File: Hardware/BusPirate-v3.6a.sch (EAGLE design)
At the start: 46 parts, among them IC1 4066, J1 USB-MINIB-5PIN, U1 MIC5205 3V3, U2 MIC5205 3V3, U3 PIC24FJ64GA002, U4 MIC5205 5V0, U5 FT232RL-BASICSSOP

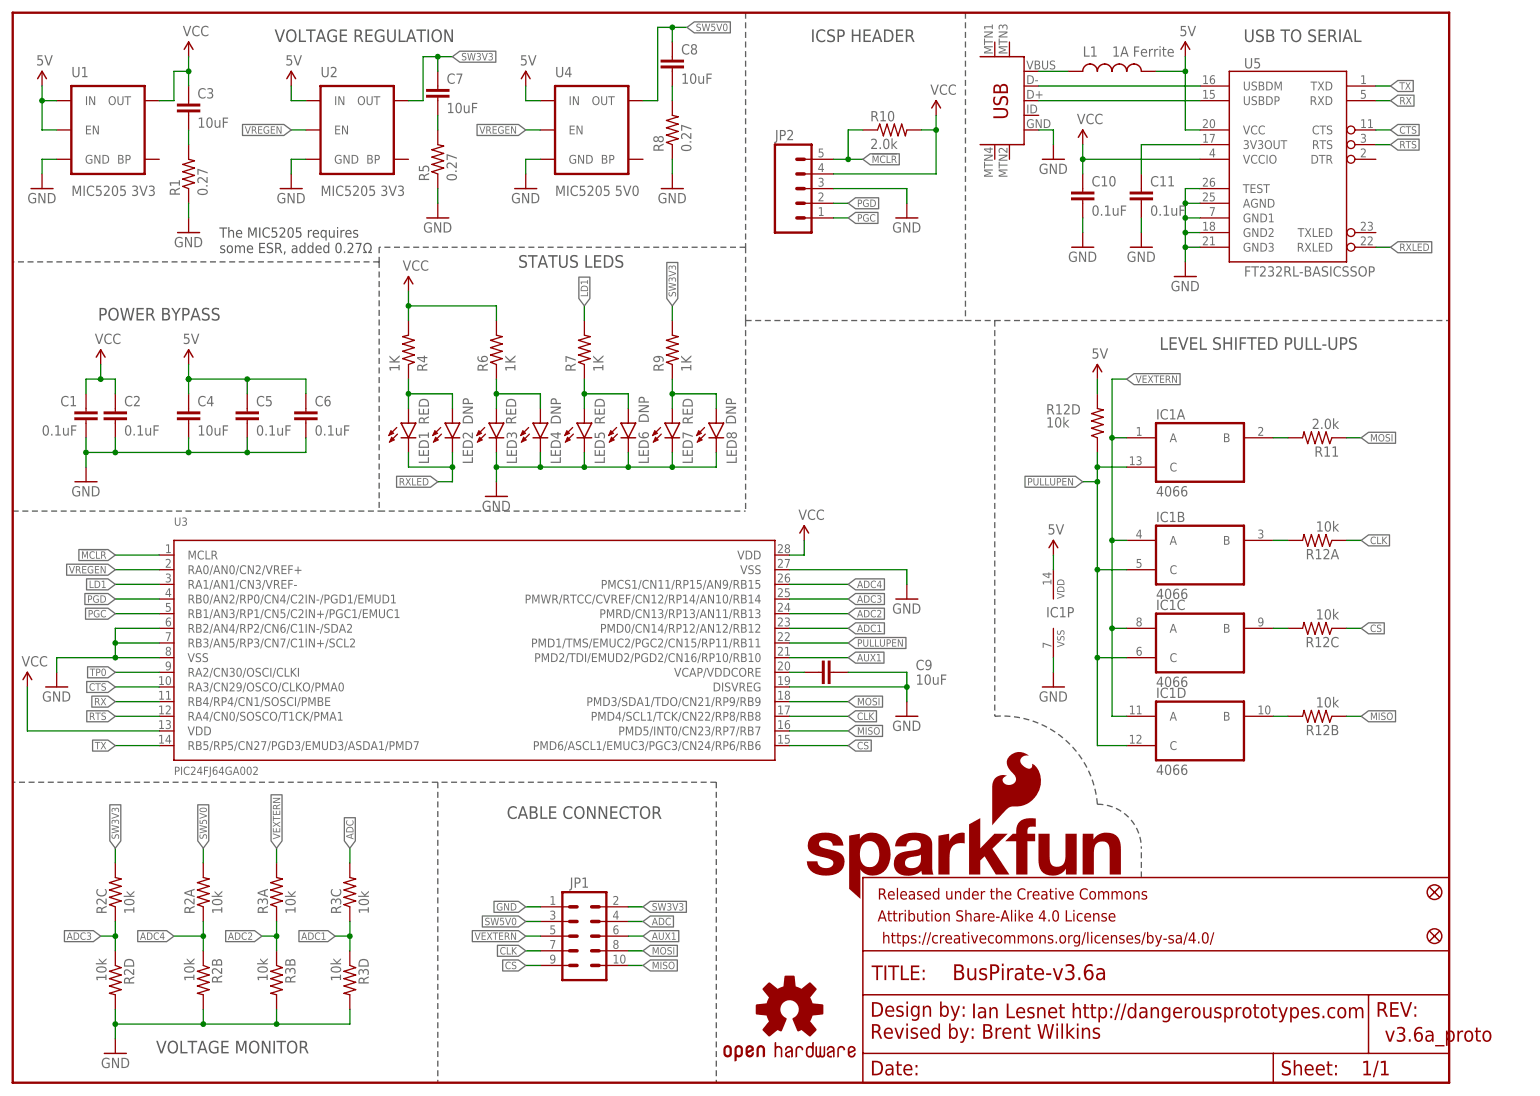
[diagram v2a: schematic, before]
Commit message: Changed license from CC4 to CC0
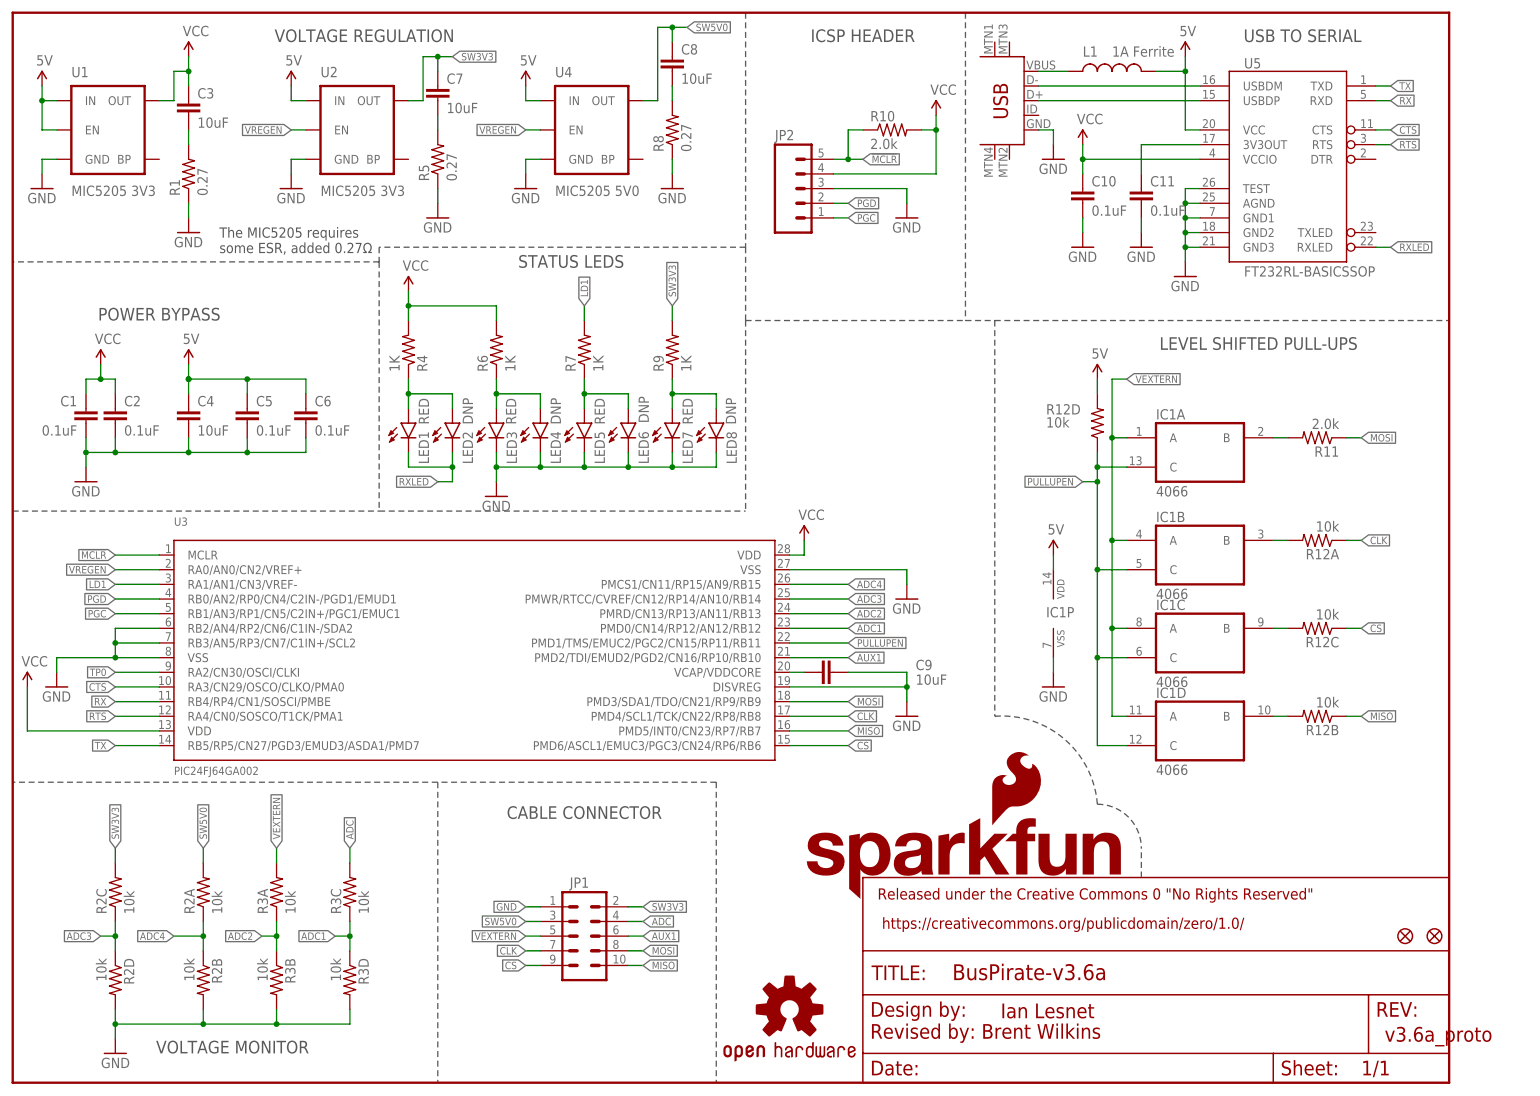
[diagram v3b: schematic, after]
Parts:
- removed FRAME1: FRAME-LETTER, SparkFun-Aesthetics:FRAME-LETTER
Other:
- note added: "Date:"
- note added: "Design by:"
- note added: "Ian Lesnet"
- note added: "REV:"
- note added: "Released under the Creative Commons 0 "No Rights Reserved""
- note added: "Sheet:"
- note added: "TITLE:"
- note added: "https://creativecommons.org/publicdomain/zero/1.0/"
- note removed: "Ian Lesnet http://dangerousprototypes.com"
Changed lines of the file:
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@@
 <part name="U2" library="SparkFun-PowerIC" deviceset="MIC5205" device="3.3V" value="MIC5205 3V3"/>
 <part name="U4" library="SparkFun-PowerIC" deviceset="MIC5205" device="5V" value="MIC5205 5V0"/>
-<part name="FRAME1" library="SparkFun-Aesthetics" deviceset="FRAME-LETTER" device=""/>
 <part name="LOGO2" library="SparkFun-Aesthetics" deviceset="SFE_LOGO_NAME_FLAME" device=".1_INCH" value="SFE_LOGO_NAME_FLAME.1_INCH"/>
 <part name="LOGO1" library="SparkFun-Aesthetics" deviceset="OSHW-LOGO" device="L" value="OSHW-LOGOL"/>
@@
 <sheet>
 <plain>
-<text x="148.59" y="7.62" size="2.54" layer="94">Revised by: Brent Wilkins</text>
-<text x="166.116" y="11.176" size="2.54" layer="94">Ian Lesnet http://dangerousprototypes.com</text>
-<text x="237.744" y="7.112" size="2.54" layer="94">v3.6a_proto</text>
+<text x="148.59" y="7.62" size="2.54" layer="94" font="vector">Revised by: Brent Wilkins</text>
+<text x="171.196" y="11.176" size="2.54" layer="94" font="vector">Ian Lesnet</text>
+<text x="237.744" y="7.112" size="2.54" layer="94" font="vector">v3.6a_proto</text>
 <text x="60.96" y="180.34" size="2.1844" layer="97" font="vector" ratio="15" align="bottom-center">VOLTAGE REGULATION</text>
 <wire x1="121.92" y1="52.07" x2="73.66" y2="52.07" width="0.1524" layer="97" style="shortdash"/>
@@
 <text x="35.814" y="143.764" size="1.778" layer="97">The MIC5205 requires
 some ESR, added 0.27Ω</text>
+<wire x1="147.32" y1="0" x2="218.44" y2="0" width="0.254" layer="94"/>
+<wire x1="248.92" y1="15.24" x2="234.95" y2="15.24" width="0.254" layer="94"/>
+<wire x1="147.32" y1="0" x2="147.32" y2="5.08" width="0.254" layer="94"/>
+<wire x1="147.32" y1="5.08" x2="218.44" y2="5.08" width="0.254" layer="94"/>
+<wire x1="147.32" y1="5.08" x2="147.32" y2="15.24" width="0.254" layer="94"/>
+<wire x1="248.92" y1="15.24" x2="248.92" y2="5.08" width="0.254" layer="94"/>
+<wire x1="218.44" y1="5.08" x2="218.44" y2="0" width="0.254" layer="94"/>
+<wire x1="218.44" y1="5.08" x2="234.95" y2="5.08" width="0.254" layer="94"/>
+<wire x1="218.44" y1="0" x2="248.92" y2="0" width="0.254" layer="94"/>
+<wire x1="234.95" y1="15.24" x2="234.95" y2="5.08" width="0.254" layer="94"/>
+<wire x1="234.95" y1="15.24" x2="147.32" y2="15.24" width="0.254" layer="94"/>
+<wire x1="234.95" y1="5.08" x2="248.92" y2="5.08" width="0.254" layer="94"/>
+<wire x1="248.92" y1="5.08" x2="248.92" y2="0" width="0.254" layer="94"/>
+<wire x1="147.32" y1="15.24" x2="147.32" y2="22.86" width="0.254" layer="94"/>
+<wire x1="248.92" y1="35.56" x2="147.32" y2="35.56" width="0.254" layer="94"/>
+<wire x1="248.92" y1="35.56" x2="248.92" y2="22.86" width="0.254" layer="94"/>
+<wire x1="147.32" y1="22.86" x2="248.92" y2="22.86" width="0.254" layer="94"/>
+<wire x1="147.32" y1="22.86" x2="147.32" y2="35.56" width="0.254" layer="94"/>
+<wire x1="248.92" y1="22.86" x2="248.92" y2="15.24" width="0.254" layer="94"/>
+<text x="148.59" y="1.27" size="2.54" layer="94" font="vector">Date:</text>
+<text x="160.02" y="1.27" size="2.54" layer="94" font="vector">&gt;LAST_DATE_TIME</text>
+<text x="219.71" y="1.27" size="2.54" layer="94" font="vector">Sheet:</text>
+<text x="233.68" y="1.27" size="2.54" layer="94" font="vector">&gt;SHEET</text>
+<text x="236.22" y="11.43" size="2.54" layer="94" font="vector">REV:</text>
+<text x="148.844" y="17.78" size="2.54" layer="94" font="vector">TITLE:</text>
+<text x="162.814" y="17.78" size="2.7432" layer="94" font="vector">&gt;DRAWING_NAME</text>
+<text x="149.86" y="31.75" size="1.9304" layer="94" font="vector">Released under the Creative Commons 0 "No Rights Reserved"</text>
+<text x="149.86" y="26.67" size="1.9304" layer="94" font="vector"> https://creativecommons.org/publicdomain/zero/1.0/</text>
+<text x="148.59" y="11.43" size="2.54" layer="94" font="vector">Design by:</text>
+<wire x1="0" y1="0" x2="0" y2="185.42" width="0.4064" layer="94"/>
+<wire x1="0" y1="185.42" x2="248.92" y2="185.42" width="0.4064" layer="94"/>
+<wire x1="248.92" y1="185.42" x2="248.92" y2="0" width="0.4064" layer="94"/>
+<wire x1="248.92" y1="0" x2="0" y2="0" width="0.4064" layer="94"/>
 </plain>
 <instances>
@@
 <instance part="U2" gate="G$1" x="60.96" y="165.1"/>
 <instance part="U4" gate="G$1" x="101.6" y="165.1"/>
-<instance part="FRAME1" gate="G$1" x="0" y="0"/>
-<instance part="FRAME1" gate="V" x="147.32" y="0"/>
 <instance part="LOGO2" gate="G$1" x="136.906" y="31.496"/>
 <instance part="LOGO1" gate="G$1" x="134.62" y="12.7"/>
@@
 <instance part="J1" gate="G$1" x="175.26" y="165.1" rot="MR0"/>
 <instance part="GND14" gate="1" x="180.34" y="160.02"/>
-<instance part="FID1" gate="G$1" x="246.38" y="33.02"/>
+<instance part="FID1" gate="G$1" x="241.3" y="25.4"/>
 <instance part="FID2" gate="G$1" x="246.38" y="25.4"/>
 <instance part="SUPPLY14" gate="G$1" x="203.2" y="177.8"/>

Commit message: Addressed issues
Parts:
- R1, R5, R8: value 0.27 -> 0
- renumbered IC1 to U6
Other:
- moved on the sheet: JP1
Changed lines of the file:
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@@
 <attribute name="PROD_ID" value="NDUC-12579"/>
 </part>
-<part name="IC1" library="40xx" deviceset="4066" device="">
+<part name="U6" library="40xx" deviceset="4066" device="">
 <attribute name="PROD_ID" value="IC-09427"/>
 </part>
@@
 <attribute name="PROD_ID" value="CONN-09508"/>
 </part>
-<part name="R1" library="SparkFun-Resistors" deviceset="0OHM-1/10W-5%(0603)" device="" value="0.27">
+<part name="R1" library="SparkFun-Resistors" deviceset="0OHM-1/10W-5%(0603)" device="" value="0">
 <attribute name="PROD_ID" value="RES-08787"/>
 </part>
-<part name="R5" library="SparkFun-Resistors" deviceset="0OHM-1/10W-5%(0603)" device="" value="0.27">
+<part name="R5" library="SparkFun-Resistors" deviceset="0OHM-1/10W-5%(0603)" device="" value="0">
 <attribute name="PROD_ID" value="RES-08787"/>
 </part>
-<part name="R8" library="SparkFun-Resistors" deviceset="0OHM-1/10W-5%(0603)" device="" value="0.27">
+<part name="R8" library="SparkFun-Resistors" deviceset="0OHM-1/10W-5%(0603)" device="" value="0">
 <attribute name="PROD_ID" value="RES-08787"/>
 </part>
@@
 <part name="C11" library="SparkFun-Capacitors" deviceset="0.1UF-25V(+80/-20%)(0603)" device="" value="0.1uF"/>
 <part name="C4" library="SparkFun-Capacitors" deviceset="10UF10V10%(0805)" device="" value="10uF"/>
+<part name="GND19" library="SparkFun-Aesthetics" deviceset="GND" device=""/>
 </parts>
 <sheets>
@@
 <attribute name="PROD_ID" x="190.5" y="175.26" size="1.778" layer="96" rot="R90" display="off"/>
 </instance>
-<instance part="IC1" gate="A" x="205.74" y="109.22"/>
-<instance part="IC1" gate="B" x="205.74" y="91.44">
+<instance part="U6" gate="A" x="205.74" y="109.22"/>
+<instance part="U6" gate="B" x="205.74" y="91.44">
 <attribute name="PROD_ID" x="205.74" y="91.44" size="1.778" layer="96" display="off"/>
 </instance>
-<instance part="IC1" gate="C" x="205.74" y="76.2"/>
-<instance part="IC1" gate="D" x="205.74" y="60.96"/>
-<instance part="IC1" gate="P" x="180.34" y="81.28"/>
+<instance part="U6" gate="C" x="205.74" y="76.2"/>
+<instance part="U6" gate="D" x="205.74" y="60.96"/>
+<instance part="U6" gate="P" x="180.34" y="81.28"/>
 <instance part="GND15" gate="1" x="180.34" y="68.58"/>
 <instance part="C6" gate="G$1" x="50.8" y="114.3"/>
@@
 </instance>
 <instance part="GND18" gate="1" x="203.2" y="139.7"/>
-<instance part="J1" gate="G$1" x="175.26" y="165.1" rot="MR0"/>
+<instance part="J1" gate="G$1" x="175.26" y="165.1" smashed="yes" rot="MR0">
+<attribute name="NAME" x="170.18" y="175.26" size="1.778" layer="95" rot="MR0"/>
+<attribute name="VALUE" x="173.482" y="184.15" size="1.778" layer="96" rot="MR180"/>
+</instance>
 <instance part="GND14" gate="1" x="180.34" y="160.02"/>
 <instance part="FID1" gate="G$1" x="241.3" y="25.4"/>
@@
 <instance part="SUPPLY10" gate="G$1" x="160.02" y="167.64"/>
 <instance part="JP2" gate="G$1" x="134.62" y="154.94"/>
-<instance part="JP1" gate="G$1" x="99.06" y="25.4">
-<attribute name="PROD_ID" x="99.06" y="25.4" size="1.778" layer="96" display="off"/>
+<instance part="JP1" gate="G$1" x="99.06" y="25.4" rot="R180">
+<attribute name="PROD_ID" x="99.06" y="25.4" size="1.778" layer="96" rot="R180" display="off"/>
 </instance>
 <instance part="R1" gate="G$1" x="30.48" y="157.48" rot="R90"/>
@@
 <instance part="C11" gate="G$1" x="195.58" y="152.4"/>
 <instance part="C4" gate="G$1" x="30.48" y="114.3"/>
+<instance part="GND19" gate="1" x="109.22" y="15.24" rot="MR0"/>
 </instances>
 <busses>
@@
 <pinref part="GND15" gate="1" pin="GND"/>
 <wire x1="180.34" y1="71.12" x2="180.34" y2="73.66" width="0.1524" layer="91"/>
-<pinref part="IC1" gate="P" pin="VSS"/>
+<pinref part="U6" gate="P" pin="VSS"/>
 </segment>
 <segment>
@@
 </segment>
 <segment>
-<label x="88.9" y="30.48" size="1.27" layer="95" rot="R180" xref="yes"/>
-<wire x1="88.9" y1="30.48" x2="91.44" y2="30.48" width="0.1524" layer="91"/>
+<wire x1="109.22" y1="20.32" x2="106.68" y2="20.32" width="0.1524" layer="91"/>
 <pinref part="JP1" gate="G$1" pin="1"/>
+<pinref part="GND19" gate="1" pin="GND"/>
+<wire x1="109.22" y1="20.32" x2="109.22" y2="17.78" width="0.1524" layer="91"/>
 </segment>
 <segment>
@@
 </segment>
 <segment>
-<label x="88.9" y="22.86" size="1.27" layer="95" rot="R180" xref="yes"/>
+<label x="109.22" y="27.94" size="1.27" layer="95" xref="yes"/>
 <pinref part="JP1" gate="G$1" pin="7"/>
-<wire x1="88.9" y1="22.86" x2="91.44" y2="22.86" width="0.1524" layer="91"/>
+<wire x1="109.22" y1="27.94" x2="106.68" y2="27.94" width="0.1524" layer="91"/>
 </segment>
 <segment>
@@
 </segment>
 <segment>
-<label x="109.22" y="20.32" size="1.27" layer="95" xref="yes"/>
+<label x="88.9" y="30.48" size="1.27" layer="95" rot="R180" xref="yes"/>
 <pinref part="JP1" gate="G$1" pin="10"/>
-<wire x1="106.68" y1="20.32" x2="109.22" y2="20.32" width="0.1524" layer="91"/>
+<wire x1="91.44" y1="30.48" x2="88.9" y2="30.48" width="0.1524" layer="91"/>
 </segment>
 <segment>
@@
 </segment>
 <segment>
-<label x="88.9" y="20.32" size="1.27" layer="95" rot="R180" xref="yes"/>
+<label x="109.22" y="30.48" size="1.27" layer="95" xref="yes"/>
 <pinref part="JP1" gate="G$1" pin="9"/>
-<wire x1="88.9" y1="20.32" x2="91.44" y2="20.32" width="0.1524" layer="91"/>
+<wire x1="109.22" y1="30.48" x2="106.68" y2="30.48" width="0.1524" layer="91"/>
 </segment>
 <segment>
@@
 </segment>
 <segment>
-<label x="109.22" y="22.86" size="1.27" layer="95" xref="yes"/>
+<label x="88.9" y="27.94" size="1.27" layer="95" rot="R180" xref="yes"/>
 <pinref part="JP1" gate="G$1" pin="8"/>
-<wire x1="106.68" y1="22.86" x2="109.22" y2="22.86" width="0.1524" layer="91"/>
+<wire x1="91.44" y1="27.94" x2="88.9" y2="27.94" width="0.1524" layer="91"/>
 </segment>
 <segment>
@@
 </segment>
 <segment>
-<label x="88.9" y="25.4" size="1.27" layer="95" rot="R180" xref="yes"/>
+<label x="109.22" y="25.4" size="1.27" layer="95" xref="yes"/>
 <pinref part="JP1" gate="G$1" pin="5"/>
-<wire x1="88.9" y1="25.4" x2="91.44" y2="25.4" width="0.1524" layer="91"/>
+<wire x1="109.22" y1="25.4" x2="106.68" y2="25.4" width="0.1524" layer="91"/>
 </segment>
 <segment>
@@
 <junction x="190.5" y="93.98"/>
 <junction x="190.5" y="111.76"/>
-<pinref part="IC1" gate="D" pin="A"/>
-<pinref part="IC1" gate="C" pin="A"/>
-<pinref part="IC1" gate="B" pin="A"/>
-<pinref part="IC1" gate="A" pin="A"/>
+<pinref part="U6" gate="D" pin="A"/>
+<pinref part="U6" gate="C" pin="A"/>
+<pinref part="U6" gate="B" pin="A"/>
+<pinref part="U6" gate="A" pin="A"/>
 <label x="193.04" y="121.92" size="1.27" layer="95" xref="yes"/>
 </segment>
@@
 </segment>
 <segment>
-<label x="109.22" y="27.94" size="1.27" layer="95" xref="yes"/>
+<label x="88.9" y="22.86" size="1.27" layer="95" rot="R180" xref="yes"/>
 <pinref part="JP1" gate="G$1" pin="4"/>
-<wire x1="106.68" y1="27.94" x2="109.22" y2="27.94" width="0.1524" layer="91"/>
+<wire x1="91.44" y1="22.86" x2="88.9" y2="22.86" width="0.1524" layer="91"/>
 </segment>
 </net>
@@
 </segment>
 <segment>
-<label x="109.22" y="30.48" size="1.27" layer="95" xref="yes"/>
+<label x="88.9" y="20.32" size="1.27" layer="95" rot="R180" xref="yes"/>
 <pinref part="JP1" gate="G$1" pin="2"/>
-<wire x1="106.68" y1="30.48" x2="109.22" y2="30.48" width="0.1524" layer="91"/>
+<wire x1="91.44" y1="20.32" x2="88.9" y2="20.32" width="0.1524" layer="91"/>
 </segment>
 <segment>
@@
 </segment>
 <segment>
-<label x="88.9" y="27.94" size="1.27" layer="95" rot="R180" xref="yes"/>
+<label x="109.22" y="22.86" size="1.27" layer="95" xref="yes"/>
 <pinref part="JP1" gate="G$1" pin="3"/>
-<wire x1="88.9" y1="27.94" x2="91.44" y2="27.94" width="0.1524" layer="91"/>
+<wire x1="109.22" y1="22.86" x2="106.68" y2="22.86" width="0.1524" layer="91"/>
 </segment>
 </net>
@@
 </segment>
 <segment>
-<label x="109.22" y="25.4" size="1.27" layer="95" xref="yes"/>
+<label x="88.9" y="25.4" size="1.27" layer="95" rot="R180" xref="yes"/>
 <pinref part="JP1" gate="G$1" pin="6"/>
-<wire x1="106.68" y1="25.4" x2="109.22" y2="25.4" width="0.1524" layer="91"/>
+<wire x1="91.44" y1="25.4" x2="88.9" y2="25.4" width="0.1524" layer="91"/>
 </segment>
 </net>
@@
 <junction x="187.96" y="73.66"/>
 <junction x="187.96" y="106.68"/>
-<pinref part="IC1" gate="B" pin="C"/>
-<pinref part="IC1" gate="C" pin="C"/>
-<pinref part="IC1" gate="D" pin="C"/>
+<pinref part="U6" gate="B" pin="C"/>
+<pinref part="U6" gate="C" pin="C"/>
+<pinref part="U6" gate="D" pin="C"/>
 <pinref part="R12" gate="D" pin="1"/>
-<pinref part="IC1" gate="A" pin="C"/>
+<pinref part="U6" gate="A" pin="C"/>
 <label x="185.42" y="104.14" size="1.27" layer="95" rot="R180" xref="yes"/>
 <wire x1="187.96" y1="104.14" x2="185.42" y2="104.14" width="0.1524" layer="91"/>
@@
 </segment>
 <segment>
-<pinref part="IC1" gate="P" pin="VDD"/>
+<pinref part="U6" gate="P" pin="VDD"/>
 <pinref part="SUPPLY11" gate="G$1" pin="5V"/>
 <wire x1="180.34" y1="91.44" x2="180.34" y2="88.9" width="0.1524" layer="91"/>
@@
 <net name="N$1" class="0">
 <segment>
-<pinref part="IC1" gate="A" pin="B"/>
+<pinref part="U6" gate="A" pin="B"/>
 <pinref part="R11" gate="G$1" pin="2"/>
 <wire x1="220.98" y1="111.76" x2="218.44" y2="111.76" width="0.1524" layer="91"/>
@@
 <net name="N$5" class="0">
 <segment>
-<pinref part="IC1" gate="B" pin="B"/>
+<pinref part="U6" gate="B" pin="B"/>
 <pinref part="R12" gate="A" pin="2"/>
 <wire x1="220.98" y1="93.98" x2="218.44" y2="93.98" width="0.1524" layer="91"/>
@@
 <net name="N$2" class="0">
 <segment>
-<pinref part="IC1" gate="C" pin="B"/>
+<pinref part="U6" gate="C" pin="B"/>
 <pinref part="R12" gate="C" pin="2"/>
 <wire x1="220.98" y1="78.74" x2="218.44" y2="78.74" width="0.1524" layer="91"/>
@@
 <net name="N$4" class="0">
 <segment>
-<pinref part="IC1" gate="D" pin="B"/>
+<pinref part="U6" gate="D" pin="B"/>
 <pinref part="R12" gate="B" pin="2"/>
 <wire x1="220.98" y1="63.5" x2="218.44" y2="63.5" width="0.1524" layer="91"/>
